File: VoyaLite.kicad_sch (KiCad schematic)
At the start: 72 parts, among them J1 Conn_01x02_Socket, J3 USB_C_Receptacle_USB2.0_16P, J4 Conn_01x04_Socket, Q1 NTJD1155LT1G, Q2 NTJD1155LT1G, SW1 SW_SPDT_312, SW2 SW_SPDT_312, U1 WE-TVS-82400102, U2 E73-2G4M08S1C, U3 BQ24075RGT, U4 XC6220B331MR, Y1 32.768kHz

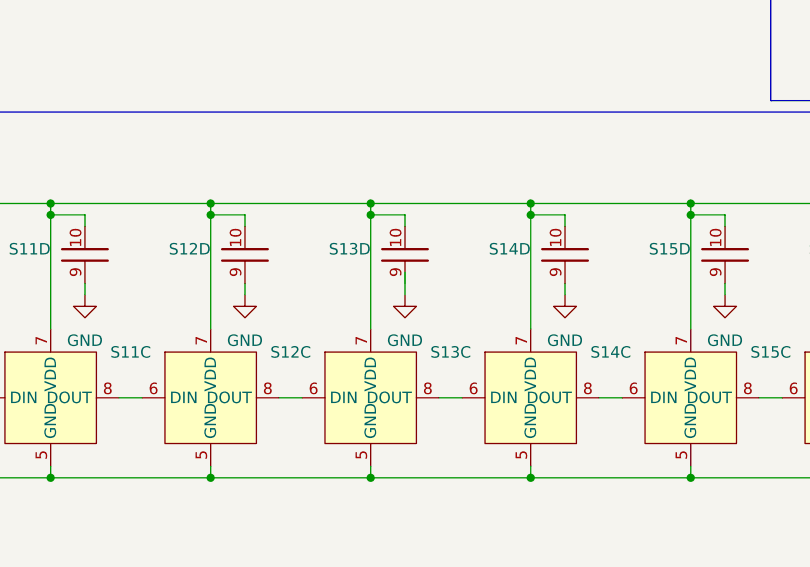
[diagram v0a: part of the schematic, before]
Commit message: add tracks
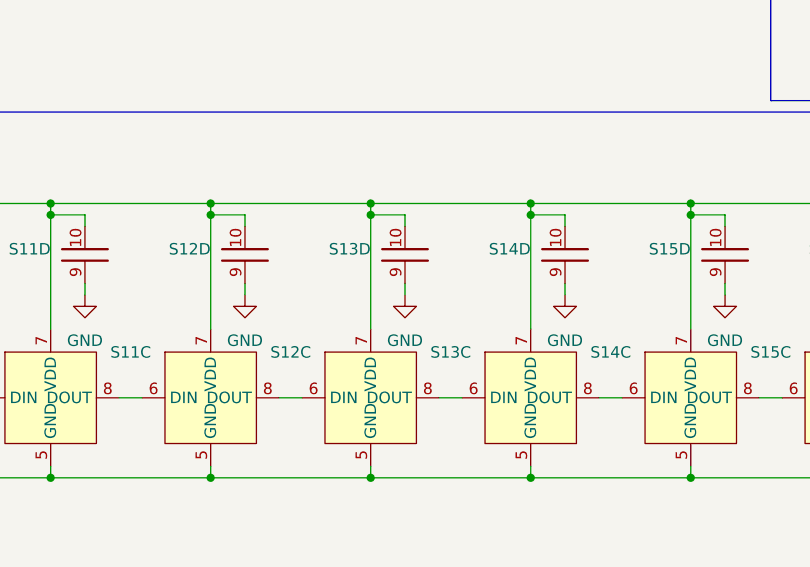
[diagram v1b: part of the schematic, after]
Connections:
- net GND: now also S13.9
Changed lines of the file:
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@@
 	(wire
 		(pts
-			(xy 248.92 203.2) (xy 248.92 205.74)
+			(xy 248.92 204.47) (xy 248.92 205.74)
 		)
 		(stroke

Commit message: add changes to voyalite. Add nrf52840 plus
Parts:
- removed C39: 4u7, Capacitor_SMD:C_0603_1608Metric_Pad1.08x0.95mm_HandSolder, symbol Device:C_Small
- added U6: XIAO-NRF82840-Plus, Module:MOUDLE14P-XIAO-DIP-SMD, symbol RT-Library-Kicad:XIAO-NRF52840-Plus
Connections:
- net +3V8: no longer C45.1, Q1.4, R6.1
- net +BATT: now also C45.1, Q1.4, R6.1, SW1.1 (B), U6.12 (P0.31/BAT/D16)
- net BAT_MEAS_ADC: now also U6.20 (P1.15/MOSI/D10)
- net BAT_MEAS_EN: now also U6.19 (P1.07/MOSI1/D19)
- net LED: now also U6.1 (P0.02/A0/D0)
- net LED_EN: now also U6.18 (P1.14/MISO/D9)
- net VBATIn: now also SW1.2 (C)
- net VCC: now also U6.23 (VBUS_5V)
- net c1: now also U6.7 (P0.29/A3/D3)
- net c2: now also U6.8 (P0.09/NFC1/RX1/D14)
- net c3: now also U6.9 (P0.04/SDA/A4/D4)
- net c4: now also U6.10 (P0.10/NFC2/TX1/D15)
- net c5: now also U6.11 (P0.05/SCL/A5/D5)
- net c6: now also U6.13 (P1.11/TX/D6)
- net c7: now also U6.14 (P1.12/RX/D7)
- net r1: now also U6.2 (P0.15/I2S_SD/D11)
- net r2: now also U6.3 (P0.03/A1/D1)
- net r3: now also U6.4 (P0.19/I2S_SCK/D12)
- net r4: now also U6.5 (P0.28/A2/D2)
- net r5: now also U6.6 (P1.01/I2S_WS/D13)
- net DP: now reaches J3.A6 (D+), J3.B6 (D+), U1.1
- net DP: now also J3.A7 (D-), J3.B7 (D-), U1.3
- net Dm: now reaches U1.4, U2.29 (DM)
- net Dp: now reaches U1.6, U2.31 (DP)
- net SWDIO: now reaches J4.3 (Pin_3), U2.37 (SWDIO)
- net SWDCLK: now reaches J4.4 (Pin_4), U2.39 (SWDCLK)
- net Y1a: now reaches C47.1, U2.11 (P0.00/XL1), Y1.2
- net Y1b: now reaches C49.1, U2.13 (P0.01/XL2), Y1.1
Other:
- note added: "VCC/GND/VBAT etc überprüfen"
- moved on the sheet: C1, C34, C36, C37, C38, C40, C41, C42, C43, C44, C47, C49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

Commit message: add newer files
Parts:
- removed C1, C34, C37, C38: 4u7, Capacitor_SMD:C_0603_1608Metric_Pad1.08x0.95mm_HandSolder, symbol Device:C_Small
- removed C36: 1u, Capacitor_SMD:C_0402_1005Metric_Pad0.74x0.62mm_HandSolder, symbol Device:C_Small
- removed C40, C43, C44: 100n, Capacitor_SMD:C_0402_1005Metric_Pad0.74x0.62mm_HandSolder, symbol Device:C_Small
- removed C41, C42: 10u, Capacitor_SMD:C_0603_1608Metric_Pad1.08x0.95mm_HandSolder, symbol Device:C_Small
- removed C47, C49: 7p, Capacitor_SMD:C_0402_1005Metric_Pad0.74x0.62mm_HandSolder, symbol Device:C_Small
- removed D1: Orange, Diode_SMD:D_0805_2012Metric_Pad1.15x1.40mm_HandSolder, symbol Device:LED
- removed J1: Conn_01x02_Socket, Connector_JST:JST_ZH_B2B-ZR_1x02_P1.50mm_Vertical, symbol Connector:Conn_01x02_Socket
- removed J3: USB_C_Receptacle_USB2.0_16P, Library_Pia:USB_C_Receptacle_Bottom_Up SMD, symbol Connector:USB_C_Receptacle_USB2.0_16P
- removed J4: Conn_01x04_Socket, Connector_PinHeader_2.54mm:PinHeader_1x04_P2.54mm_Vertical, symbol Connector:Conn_01x04_Socket
- removed JP1: SolderJumper_2_Open, Jumper:SolderJumper-2_P1.3mm_Open_TrianglePad1.0x1.5mm, symbol Jumper:SolderJumper_2_Open
- removed L1: 10uH, Inductor_SMD:L_APV_ANR5045, symbol Device:L
- removed R1, R2, R5: 10K, Capacitor_SMD:C_0402_1005Metric_Pad0.74x0.62mm_HandSolder, symbol Device:R_Small
- removed R3, R4: 51K, Capacitor_SMD:C_0402_1005Metric_Pad0.74x0.62mm_HandSolder, symbol Device:R_Small
- removed R7: 2K, Capacitor_SMD:C_0402_1005Metric_Pad0.74x0.62mm_HandSolder, symbol Device:R_Small
- removed SW1, SW2: SW_SPDT_312, Button_Switch_SMD:SW_SPDT_PCM12, symbol Switch:SW_SPDT_312
- removed U1: WE-TVS-82400102, Package_TO_SOT_SMD:SOT-23-6, symbol Power_Protection:WE-TVS-82400102
- removed U2: E73-2G4M08S1C, E73-2G4M08S1C:E73-2G4M08S1C, symbol RT-Library-Kicad:E73-2G4M08S1C
- removed U3: BQ24075RGT, Package_DFN_QFN:VQFN-16-1EP_3x3mm_P0.5mm_EP1.6x1.6mm, symbol Battery_Management:BQ24075RGT
- removed U4: XC6220B331MR, Package_TO_SOT_SMD:SOT-23-5, symbol Regulator_Linear:XC6220B331MR
- removed Y1: 32.768kHz, Crystal:Crystal_SMD_HC49-SD_HandSoldering, symbol Device:Crystal
- added BT1: Battery_Cell, Pia_Lib:Batteriehalter AAA_Metall, symbol Device:Battery_Cell
- added J1, J2: Conn_01x01_Pin, RT-Library:Testpoint-pad, symbol Connector:Conn_01x01_Pin
- Q1, Q2: footprint Library_Pia:TRANS_NTJD1155LT1G -> Pia_Lib:TRANS_NTJD1155LT1G
- S1, S10, S11, S12, S13, S14, S15, S16, S17, S18, S19, S2, S20, S21, S22, S23, S24, S25, S26, S27, S28, S29, S3, S30, S31, S4, S5, S6, S7, S8, S9: footprint Library_Pia:Kailh_Low-Profile-Switch_17mm_one Side -> Pia_Lib:Kailh_Low-Profile-Switch_17mm_one Side
- U6: footprint Module:MOUDLE14P-XIAO-DIP-SMD -> Pia_Lib:MCU_Seeed_nRF52840
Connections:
- net +BATT: now also BT1.1 (+), J1.1 (Pin_1)
- net GND: now also BT1.2 (-), J2.1 (Pin_1)
- no-connect marks 7 -> 1
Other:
- note removed: "!"
- note removed: "Battery Charger"
- note removed: "LDO"
- note removed: "USB"
- note removed: "ja"
- note removed: "uC USB"
